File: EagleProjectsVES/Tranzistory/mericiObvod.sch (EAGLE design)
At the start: 51 parts, among them IC1 TLC272P, IC2 TLC272P, IC3 NE555N, IC4 NE555N, K1 M3XXH, K2 M3XXH, K3 M3XXH, K4 M3XXH, Q1 BC557B

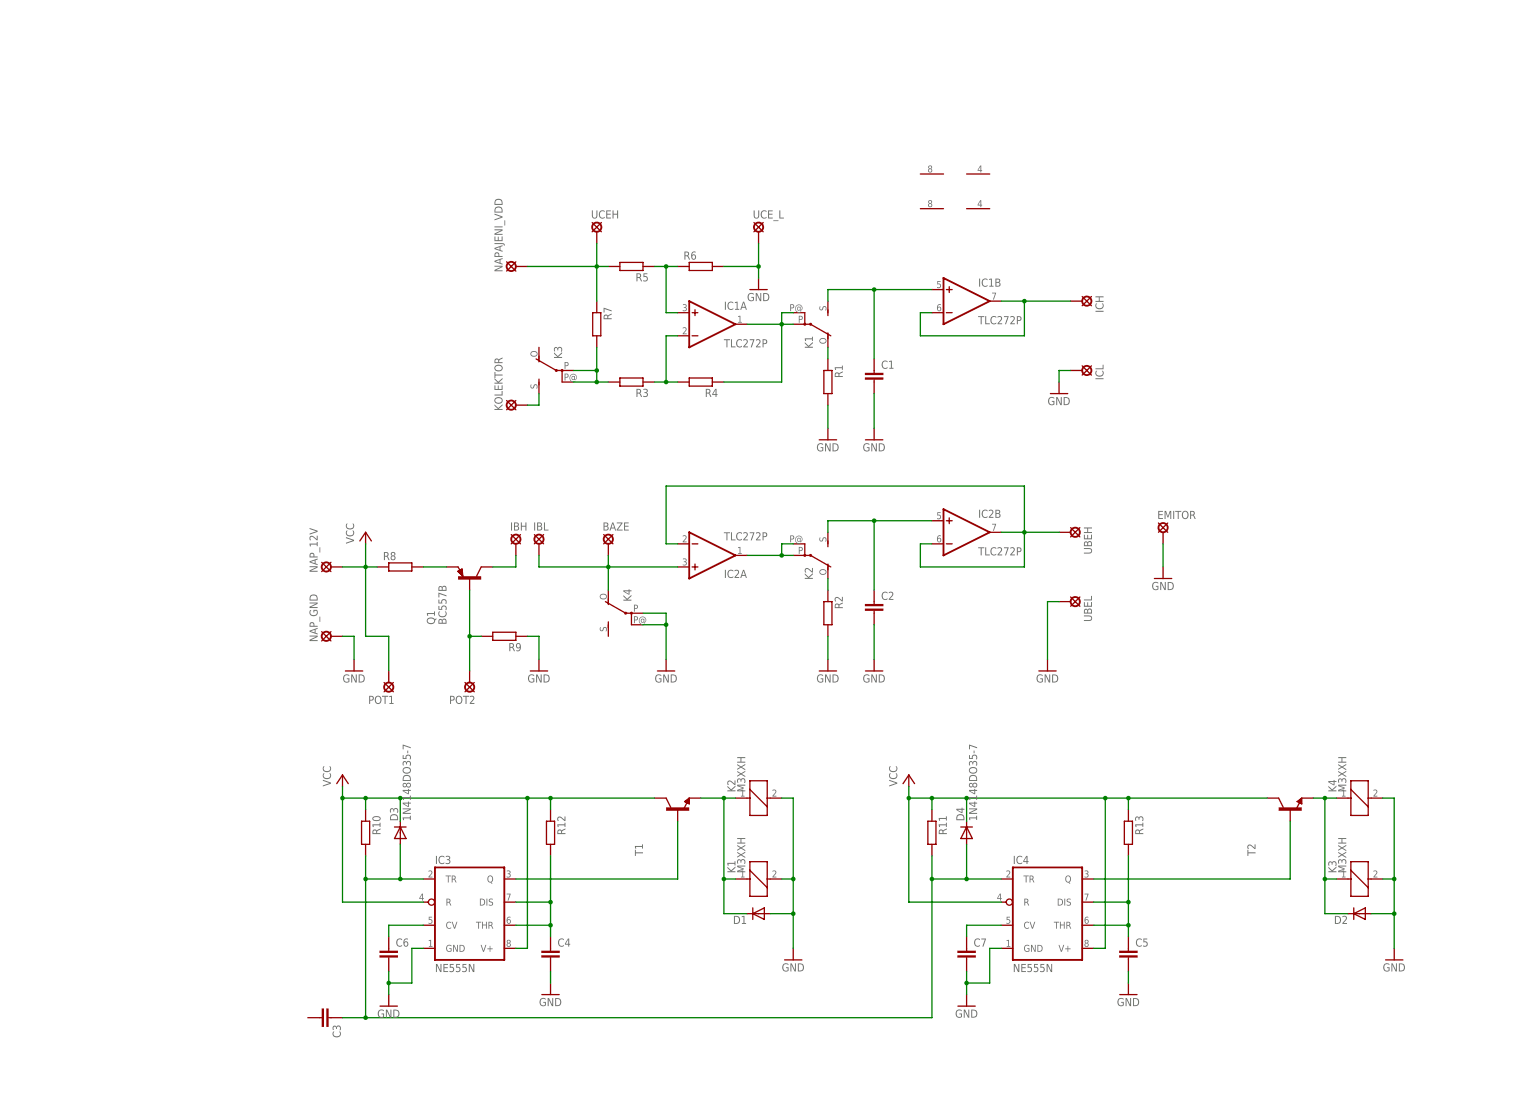
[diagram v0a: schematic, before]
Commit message: Dotvorene schema mereni tranzistoru - nutno predelat pripojne body meraku a zdroju na svorkovnice ARK
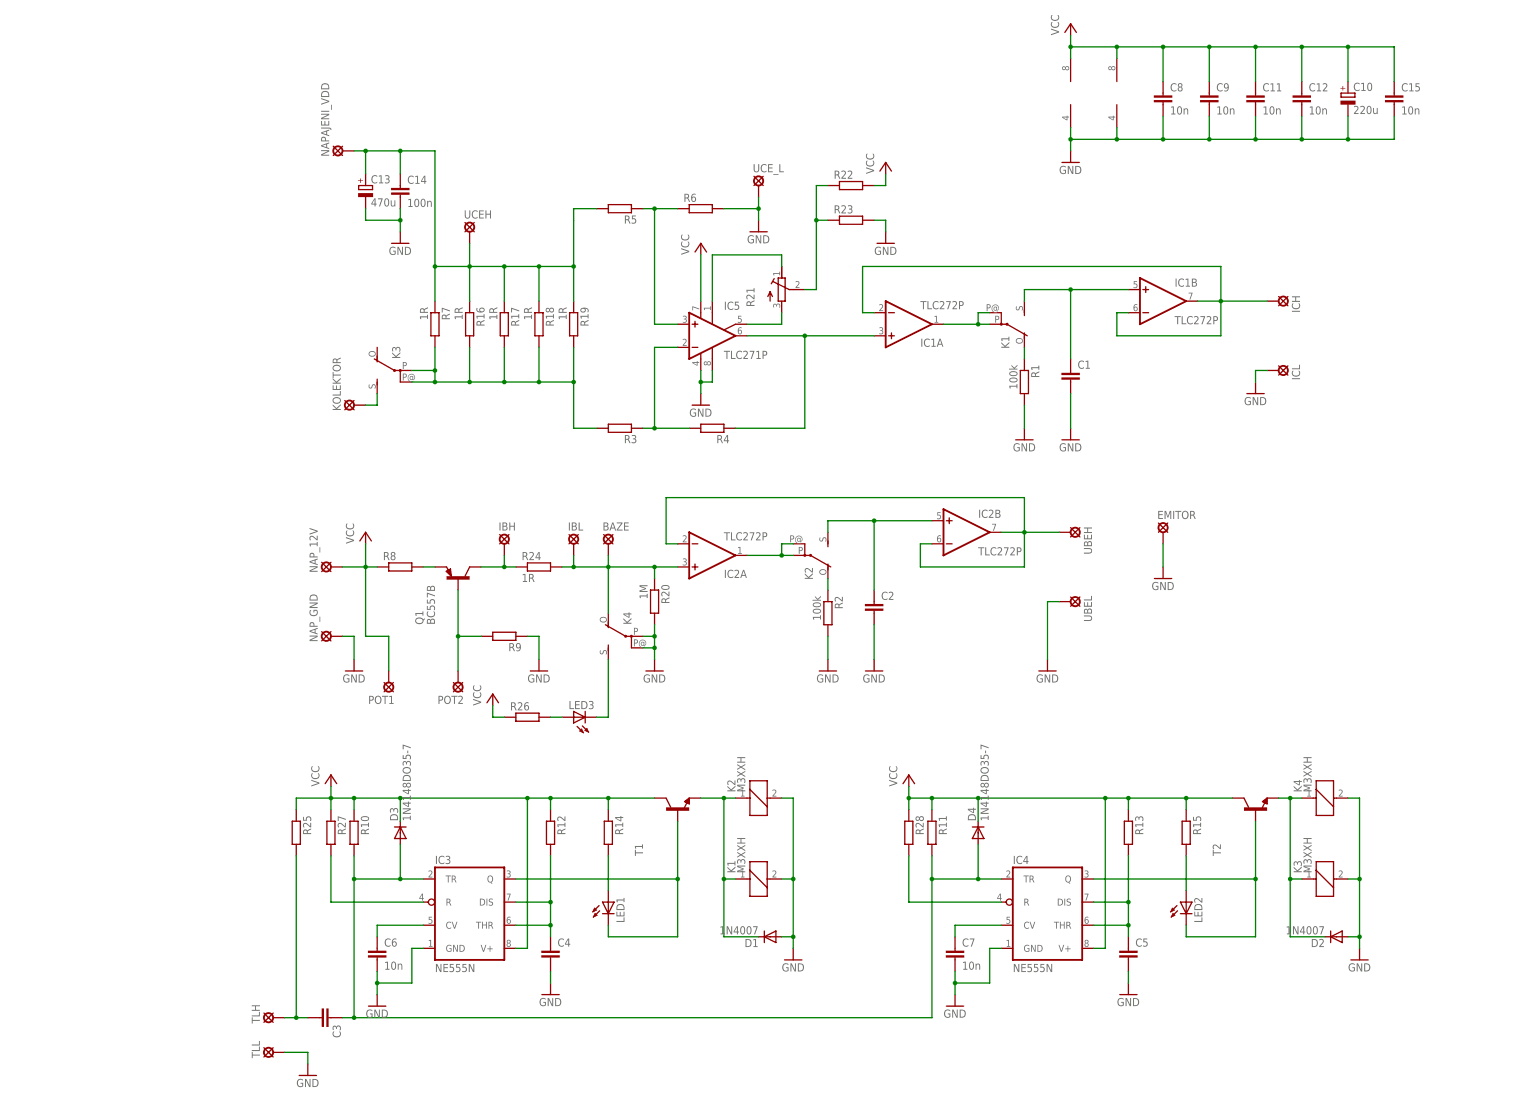
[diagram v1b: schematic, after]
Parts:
- added C10: 220u, rcl:CPOL-EUE5-8.5
- added C11, C12, C15, C8, C9: 10n, rcl:C-EU050-030X075
- added C13: 470u, rcl:CPOL-EUE5-8.5
- added C14: 100n, rcl:C-EU050-030X075
- added IC5: TLC271P, linear:TLC271P
- added LED1, LED2, LED3: (no value), led:LED3MM
- added R14, R15, R22, R23, R25, R26, R27, R28: (no value), rcl:R-EU_0207/10
- added R16, R17, R18, R19, R24: 1R, rcl:R-EU_0207/10
- added R20: 1M, rcl:R-EU_0207/10
- added R21: (no value), rcl:R-TRIMMT18
- added TLH, TLL: SE13, solpad:SE13
- C6, C7: value (none) -> 10n
- D1, D2: value (none) -> 1N4007
- R1, R2: value (none) -> 100k
- R7: value (none) -> 1R
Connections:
- new net N$23: LED1.A, R14.2
- new net N$27: IC1A.+IN, IC5.OUT, R4.1
- new net N$29: LED2.A, R15.2
- new net N$30: C3.2, R25.2, TLH.MP
- new net N$31: LED3.A, R26.2
- new net N$32: IC5.ON2, R21.A
- new net N$33: IC5.ON1, R21.E
- new net N$34: R21.S, R22.1, R23.1
- new net N$35: K42.S, LED3.C
- new net N$36: IC3.R, R27.2
- new net N$37: IC4.R, R28.2
- net GND: now also C10.-, C11.2, C12.2, C13.-, C14.2, C15.2, C8.2, C9.2, IC1P.V-, IC2P.V-, IC5.OPT, IC5.V-, R20.2, R23.2, TLL.MP
- net N$1: now also IC5.-IN; no longer IC1A.-IN
- net N$10: now also IC1A.-IN
- net N$11: now also C13.+, C14.1, R16.1, R17.1, R18.1, R19.1
- net N$12: now also R16.2, R17.2, R18.2, R19.2
- net N$13: now also R20.1, R24.2
- net N$16: now also R24.1
- net N$19: now also LED1.C
- net N$20: now also LED2.C
- net N$6: no longer R4.1
- net N$9: now also IC5.+IN; no longer IC1A.+IN
- net VCC: now also C10.+, C11.1, C12.1, C15.1, C8.1, C9.1, IC1P.V+, IC2P.V+, IC5.V+, R14.1, R15.1, R22.2, R25.1, R26.1, R27.1, R28.1; no longer IC3.R, IC4.R
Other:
- moved on the sheet: C1, C6, C7, D1, D2, D4, IBH, IBL, IC1A, IC1B, ICH, ICL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

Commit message: Predelany svorkovnice
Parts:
- removed IBH, IBL, ICH, ICL, NAPAJENI_VDD, NAP_12V, NAP_GND, POT1, POT2, TLH, TLL, UBEH, UBEL, UCEH, UCE_L: SE13, solpad:SE13
- added IB, IC, POT, TL, U12V, UBE, UCE1, UCE2: SMKDSP_1,5/2, con-phoenix-smkdsp:SMKDSP_1,5/2
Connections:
- net GND: now also IC-2.KL, TL-2.KL, U12V-2.KL, UBE-2.KL, UCE1-2.KL, UCE2-2.KL; no longer ICL.MP, NAP_GND.MP, TLL.MP, UBEL.MP, UCE_L.MP
- net N$10: now also IC-1.KL; no longer ICH.MP
- net N$11: now also UCE1-1.KL, UCE2-1.KL; no longer NAPAJENI_VDD.MP, UCEH.MP
- net N$13: now also IB-2.KL; no longer IBL.MP
- net N$15: now also POT-2.KL; no longer POT2.MP
- net N$16: now also IB-1.KL; no longer IBH.MP
- net N$2: now also UBE-1.KL; no longer UBEH.MP
- net N$30: now also TL-1.KL; no longer TLH.MP
- net VCC: now also POT-1.KL, U12V-1.KL; no longer NAP_12V.MP, POT1.MP

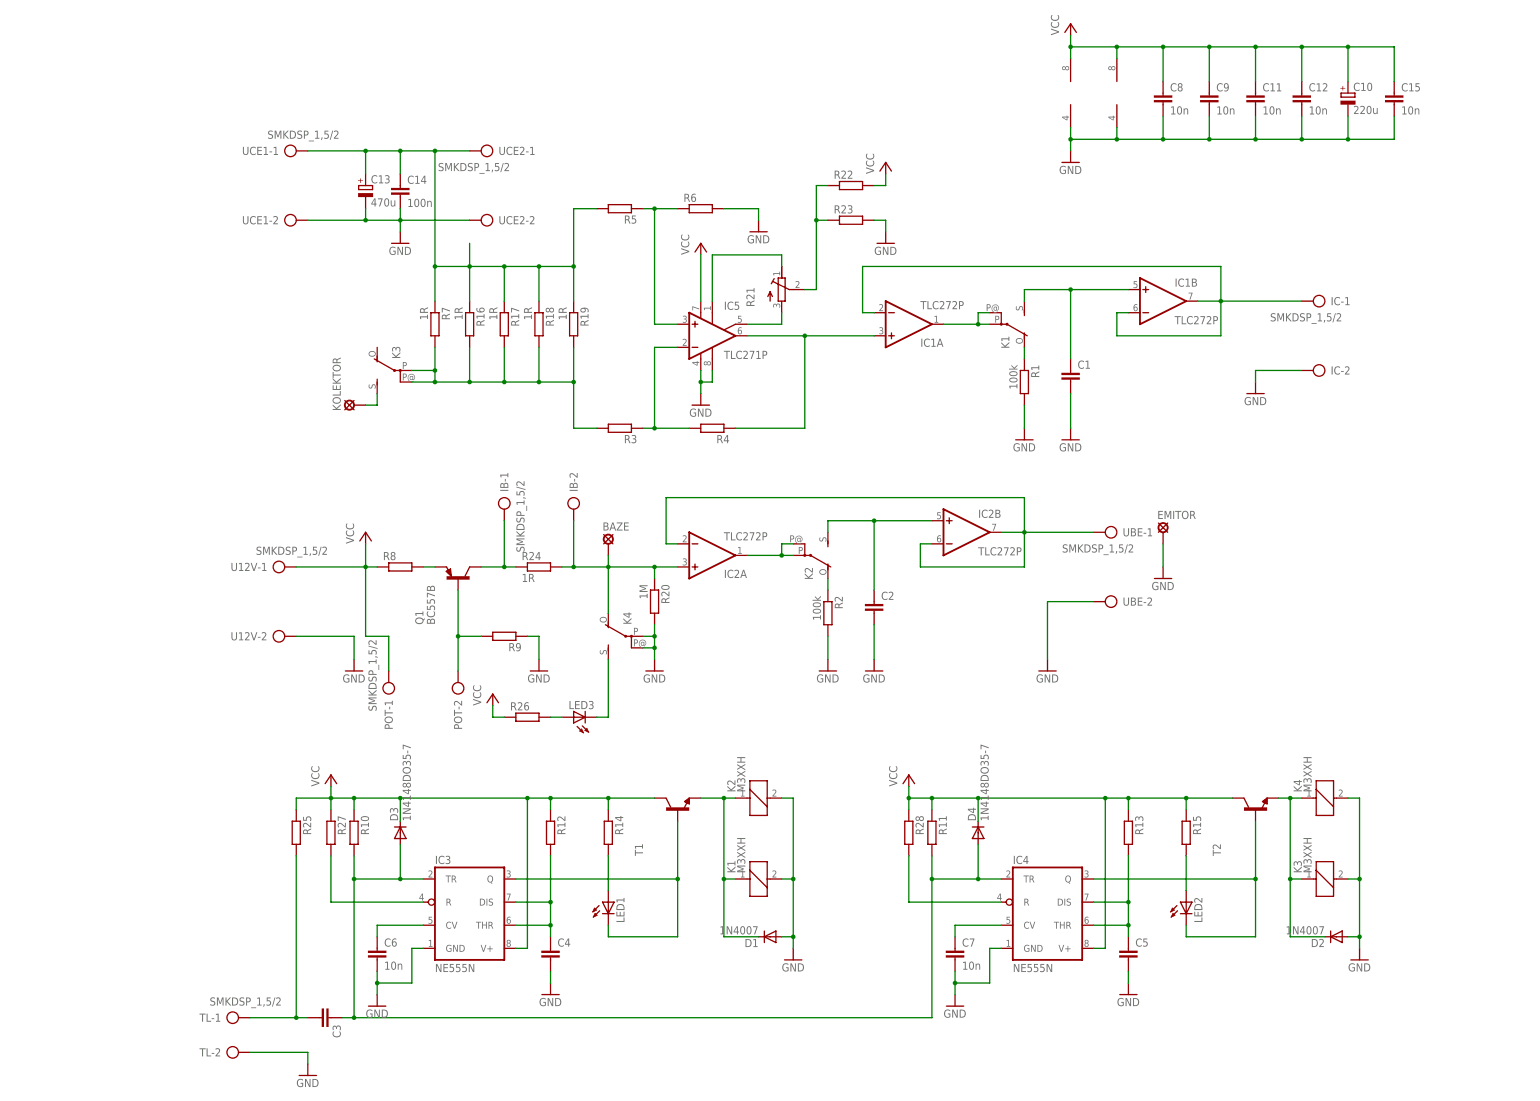
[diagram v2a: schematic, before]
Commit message: Navrzena DPS pro mereni tranzistoru. Vyroba musi byt v Pragoboardu.
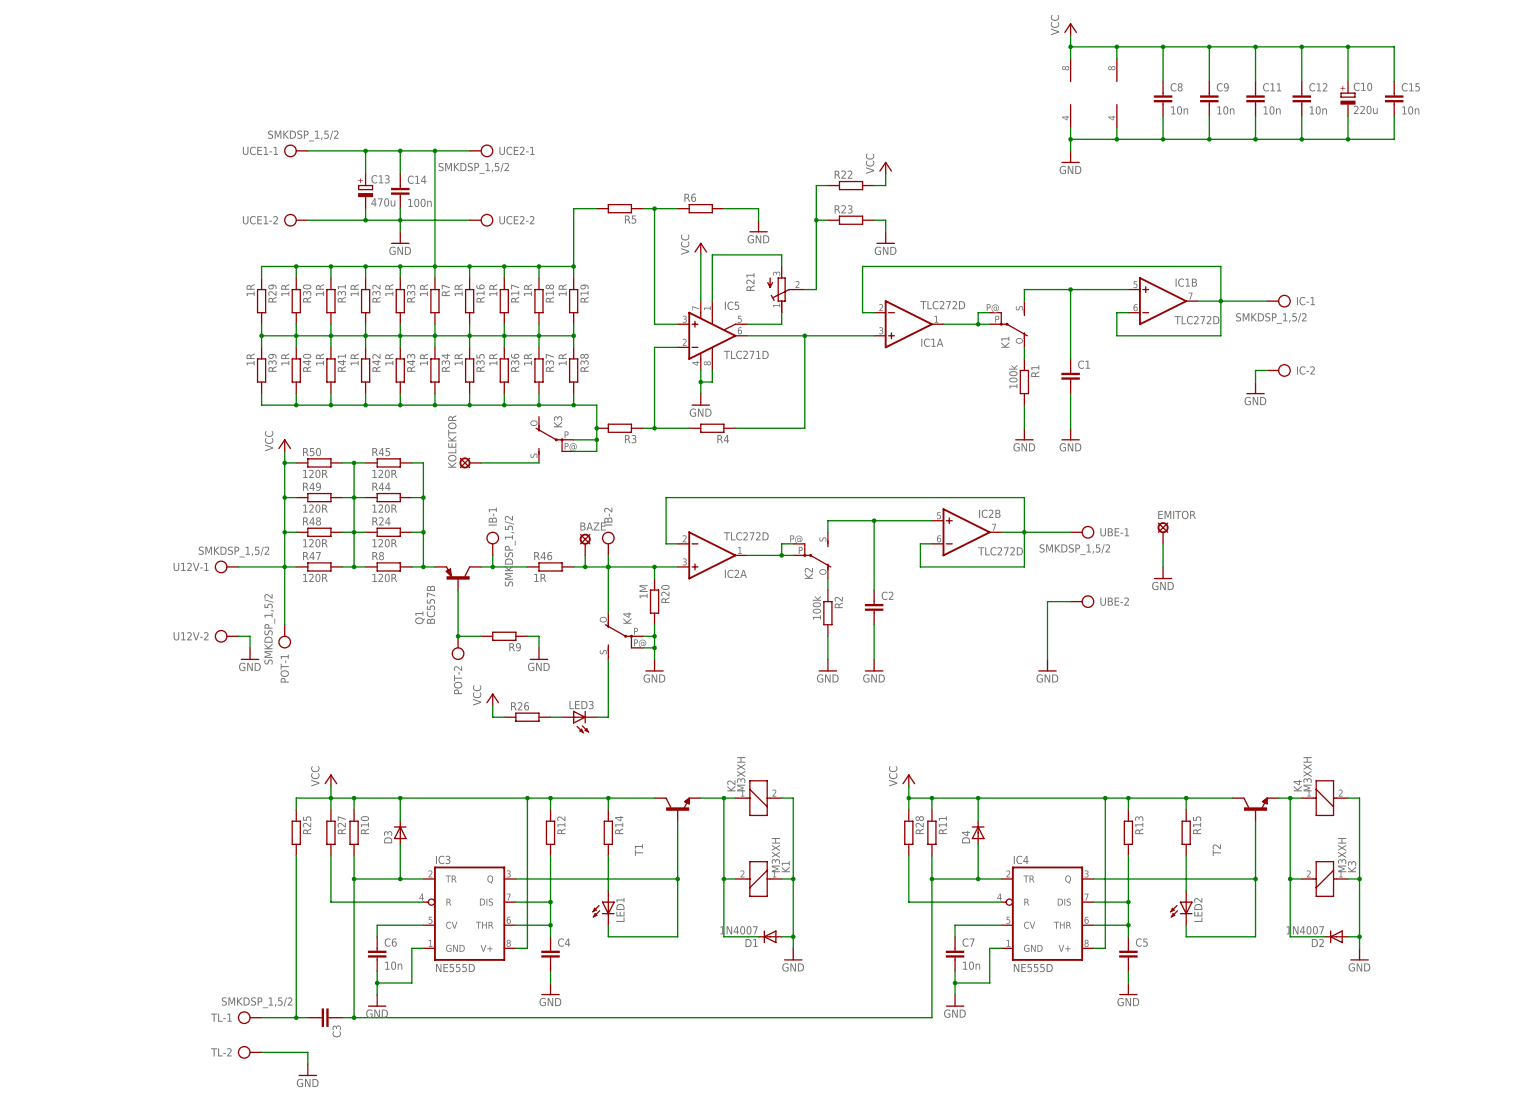
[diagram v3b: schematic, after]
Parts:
- added R29, R30, R31, R32, R33, R34, R35, R36, R37, R38, R39, R40, R41, R42, R43, R46: 1R, rcl:R-EU_R0805
- added R44, R45, R47, R48, R49, R50: 120R, rcl:R-EU_R0805
- C1, C11, C12, C15, C2, C3, C4, C5, C6, C7, C8, C9: device rcl:C-EU050-030X075 -> rcl:C-EUC0805K
- D3, D4: value 1N4148DO35-7 -> (none); device diode:1N4148DO35-7 -> semicon-smd-ipc:D-SOD-80
- IC1, IC2: value TLC272P -> TLC272D; device linear:TLC272P -> linear:TLC272D
- IC3, IC4: value NE555N -> NE555D; device linear:NE555N -> linear:NE555D
- IC5: value TLC271P -> TLC271D; device linear:TLC271P -> linear:TLC271D
- R1, R10, R11, R12, R13, R14, R15, R16, R17, R18, R19, R2, R20, R22, R23, R25, R26, R27, R28, R3, R4, R5, R6, R7, R9: device rcl:R-EU_0207/10 -> rcl:R-EU_R0805
- R24: value 1R -> 120R; device rcl:R-EU_0207/10 -> rcl:R-EU_R0805
- R8: value (none) -> 120R; device rcl:R-EU_0207/10 -> rcl:R-EU_R0805
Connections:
- new net N$48: K32.P, K32.P@1, R3.2, R34.2, R35.2, R36.2, R37.2, R38.2, R39.2, R40.2, R41.2, R42.2, R43.2
- new net N$8: R16.2, R17.2, R18.2, R19.2, R29.2, R30.2, R31.2, R32.2, R33.2, R34.1, R35.1, R36.1, R37.1, R38.1, R39.1, R40.1, R41.1, R42.1, R43.1, R7.2
- net GND: now also K11.1, K31.1; no longer K11.2, K31.2
- net N$11: now also R29.1, R30.1, R31.1, R32.1, R33.1
- net N$12: now also R24.1, R44.1, R45.1, R47.2, R48.2, R49.2, R50.2, R8.1; no longer K32.P, K32.P@1, R16.2, R17.2, R18.2, R19.2, R3.2, R7.2
- net N$13: now also R46.2; no longer R24.2
- net N$16: now also R46.1; no longer R24.1
- net N$17: now also R24.2, R44.2, R45.2
- net N$18: now also K11.2; no longer K11.1
- net N$21: now also K31.2; no longer K31.1
- net N$32: now also R21.E; no longer R21.A
- net N$33: now also R21.A; no longer R21.E
- net VCC: now also R47.1, R48.1, R49.1, R50.1; no longer R8.1
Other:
- moved on the sheet: BAZE, IB-1, IB-2, IC-1, IC-2, K3, KOLEKTOR, POT-1, POT-2, R16, R17, R18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

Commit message: Tranzistory predany k vyrobe
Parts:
- added D5: LL4148, semicon-smd-ipc:D-SOD-80
- added H1, H2, H3, H4: MOUNT-PAD-ROUND3.2, holes:MOUNT-PAD-ROUND3.2
- C1, C2, C3: value (none) -> 470n
- C4, C5: value (none) -> 10u
- D3, D4: value (none) -> LL4148
- R1, R2: value 100k -> 1M
- R10, R11, R14, R15, R25, R26, R27, R28, R3, R5: value (none) -> 2k2
- R12: value (none) -> 47k
- R13: value (none) -> 100k
- R21: value (none) -> 25k
- R22, R23, R4, R6: value (none) -> 11k
- R9: value (none) -> 5k1
- renumbered Q1 to T3
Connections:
- new net N$14: D5.A, POT-2.KL
- net GND: now also H1.MOUNT, H2.MOUNT, H3.MOUNT, H4.MOUNT
- net N$15: now also D5.C; no longer POT-2.KL
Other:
- note added: "potenciometr 5k"
- moved on the sheet: C3, K3, POT-1, POT-2, R25, R27, R28, TL-1, TL-2
